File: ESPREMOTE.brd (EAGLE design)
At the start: 48 x 78 mm, 37 parts, among them IC1 ESP12SMT, IC2 LD111733, J1 DC_2_1MM, Q1 2N7002, Q2 2N7002, Q3 2N7002, Q4 2N7002

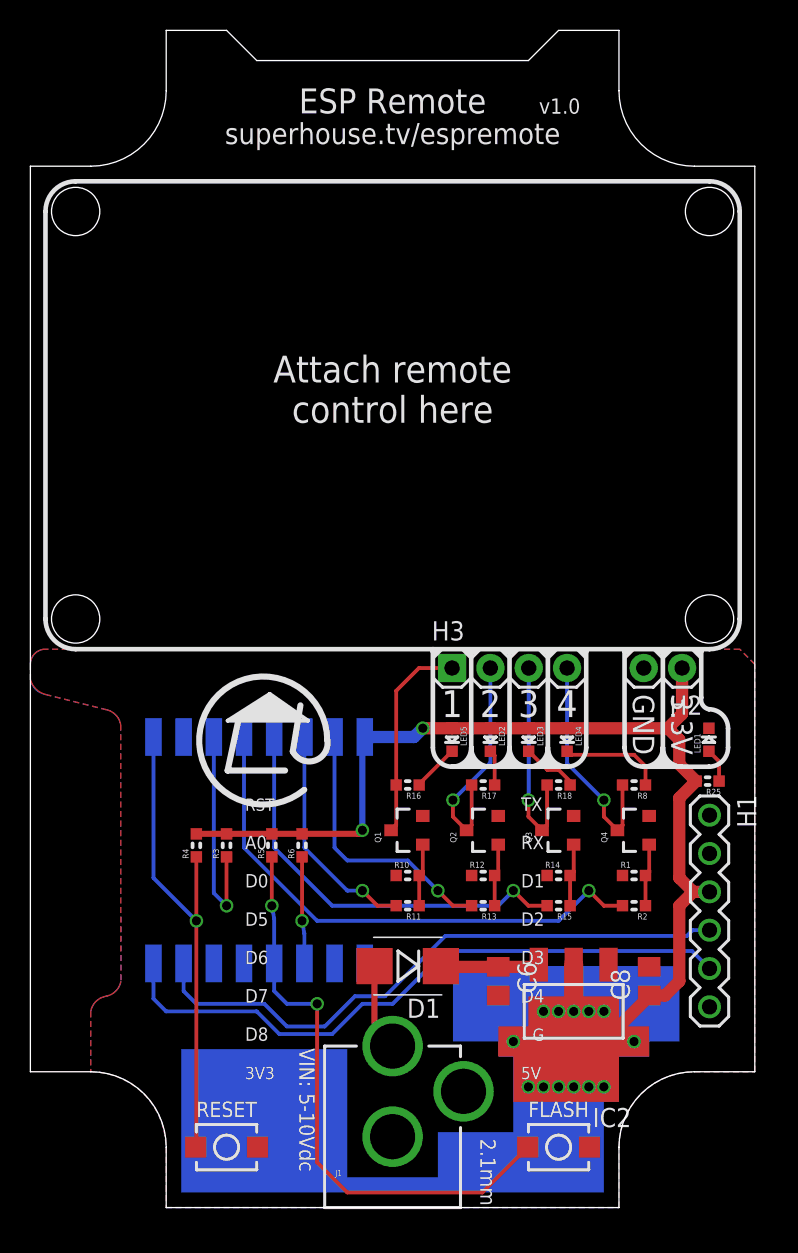
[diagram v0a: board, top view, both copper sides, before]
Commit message: Finished schematic and routing for v1.0 release
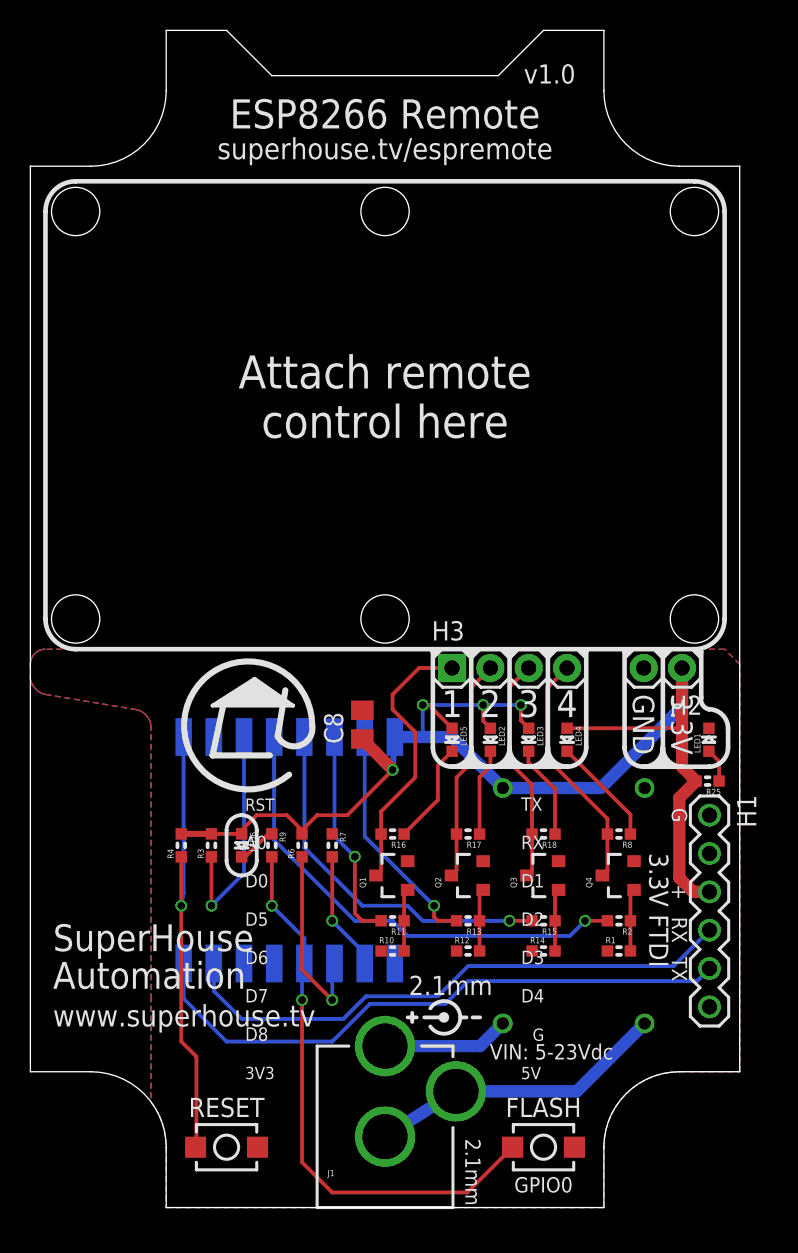
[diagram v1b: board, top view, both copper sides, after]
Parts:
- removed C6: 10uF 10V 0805, freetronics-jon:C0805
- removed D1: 1N4004 SMB, freetronics:SMB-DIODE
- removed R5: 10k, freetronics-jon:0603
- added LED6: CH1/RED, freetronics-master-v1:LED-0603
- added R7: 10k, freetronics-jon:0603
- added R9: 1K, freetronics-master-v1:0603
- IC2: value LD111733 -> REGMODULE4PIN; device freetronics-luke:SOT-223 -> freetronics-jon:REGMODULE4PIN
- moved C8 25.5 mm to (22.0, 32.0)
- moved IC2 7.00 mm to (36.0, 20.0), flipped to the bottom, turned to 90 degrees
- moved R1 5.10 mm to (39.0, 17.0)
- moved R10 5.10 mm to (24.0, 17.0)
- moved R12 5.10 mm to (29.0, 17.0)
- moved R14 5.10 mm to (34.0, 17.0)
- moved R16 3.40 mm to (24.0, 24.8)
- moved R17 3.40 mm to (29.0, 24.8)
- moved R18 3.40 mm to (34.0, 24.8)
- moved R8 3.40 mm to (39.0, 24.8)
- moved Q1 3.16 mm to (24.0, 22.0)
- moved Q2 3.16 mm to (29.0, 22.0)
- moved Q3 3.16 mm to (34.0, 22.0)
- moved Q4 3.16 mm to (39.0, 22.0)
- moved IC1 2.00 mm to (14.2, 23.7)
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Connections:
- removed net VIN: C6.1, D1.C, IC2.3
- new net N$27: LED6.C, R9.1
- new net N$28: IC2.1, J1.GND, J1.GNDBREAK
- net 3.3V: now also IC2.3, LED6.A; no longer IC2.2, IC2.4, R5.2
- net GND: now also IC2.4, R7.1; no longer C6.2, IC2.1, J1.GND, J1.GNDBREAK
- net GPIO0: now also R9.2; no longer R5.1
- net GPIO15: now also R7.2
- net N$8: now also IC2.2; no longer D1.A
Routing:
- net N$28: track 0.00 -> 19.9 mm
- net 3.3V: track 77.4 -> 87.0 mm, vias 3 -> 4
- net GPIO15: track 0.00 -> 7.95 mm, vias 0 -> 1
- net VIN: track 6.57 -> 0.00 mm
- net GPIO2: track 7.07 -> 12.8 mm
- net N$5: track 13.7 -> 18.4 mm
- net GPIO16: track 35.7 -> 32.0 mm
- net N$24: track 3.14 -> 6.80 mm
- net N$21: track 2.35 -> 5.79 mm
- net GPIO14: track 27.8 -> 24.4 mm
- net N$27: track 0.00 -> 2.63 mm
- net N$8: track 5.80 -> 8.42 mm
- net GPIO13: track 18.0 -> 15.4 mm
- net TX: track 42.9 -> 40.4 mm
- net N$4: track 3.81 -> 6.23 mm
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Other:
- board size 48 x 78 mm -> 47 x 78 mm
- board text added: "+"
- board text added: "3.3V FTDI"
- board text added: "ESP8266 Remote"
- board text added: "GPIO0"
- board text added: "Licensed under the terms of the TAPR Open Hardware Licence: tapr.org/ohl"
- board text added: "SuperHouse Automation"
- board text added: "VIN: 5-23Vdc"
- board text added: "www.superhouse.tv"
- board text removed: "ESP Remote"
- board text removed: "VIN: 5-10Vdc"

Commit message: Final silkscreen and label improvements for v1.0 release
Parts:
- LED6: value CH1/RED -> GREEN

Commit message: Added output info to silkscreen
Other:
- board text added: "Arduino board profile: "Generic ESP8266 Module""
- board text added: "Licensed under the TAPR Open Hardware Licence: tapr.org/ohl"
- board text added: "Output 1: GPIO12 Output 2: GPIO13 Output 3: GPIO14 Output 4: GPIO16"
- board text removed: "Arduino board profile: Generic ESP8266"
- board text removed: "Licensed under the terms of the TAPR Open Hardware Licence: tapr.org/ohl"
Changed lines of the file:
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@@
 <layer number="14" name="Route14" color="1" fill="6" visible="no" active="no"/>
 <layer number="15" name="Route15" color="4" fill="6" visible="no" active="no"/>
-<layer number="16" name="Bottom" color="1" fill="1" visible="no" active="yes"/>
+<layer number="16" name="Bottom" color="1" fill="1" visible="yes" active="yes"/>
 <layer number="17" name="Pads" color="2" fill="1" visible="yes" active="yes"/>
 <layer number="18" name="Vias" color="2" fill="1" visible="yes" active="yes"/>
 <layer number="19" name="Unrouted" color="12" fill="1" visible="yes" active="yes"/>
 <layer number="20" name="Dimension" color="15" fill="1" visible="yes" active="yes"/>
-<layer number="21" name="tPlace" color="15" fill="1" visible="no" active="yes"/>
-<layer number="22" name="bPlace" color="14" fill="1" visible="no" active="yes"/>
+<layer number="21" name="tPlace" color="15" fill="1" visible="yes" active="yes"/>
+<layer number="22" name="bPlace" color="14" fill="1" visible="yes" active="yes"/>
 <layer number="23" name="tOrigins" color="15" fill="1" visible="yes" active="yes"/>
 <layer number="24" name="bOrigins" color="3" fill="1" visible="yes" active="yes"/>
@@
 <text x="14.224" y="13.589" size="0.889" layer="25" font="vector" ratio="15">D7</text>
 <text x="14.224" y="21.209" size="0.889" layer="25" font="vector" ratio="15">D0</text>
-<text x="34.186" y="52.9" size="1.27" layer="22" font="vector" ratio="12" distance="36" rot="MR0">(C)2017 SuperHouse
+<text x="35.186" y="67.9" size="1.5" layer="22" font="vector" ratio="12" distance="36" rot="MR0">(C)2017 SuperHouse
 Automation Pty Ltd</text>
 <text x="23.5" y="71.5" size="1.9304" layer="21" font="vector" ratio="18" distance="40" rot="SR0" align="bottom-center">ESP8266 Remote</text>
@@
 <text x="30.438" y="9.814" size="1.016" layer="21" font="vector" ratio="13" rot="SR0">VIN: 5-23Vdc</text>
 <text x="13" y="6" size="1.27" layer="21" font="vector" ratio="18" distance="40" rot="SR0" align="bottom-center">RESET</text>
-<text x="34.186" y="61.158" size="1.27" layer="22" font="vector" ratio="15" rot="MR0">Arduino board profile:
-Generic ESP8266</text>
+<text x="40.186" y="59.158" size="1.7" layer="22" font="vector" ratio="15" rot="MR0">Arduino board profile:
+"Generic ESP8266 Module"</text>
 <wire x1="46" y1="66" x2="44" y2="68" width="0.3048" layer="21" curve="90"/>
 <wire x1="44" y1="68" x2="3" y2="68" width="0.3048" layer="21"/>
@@
 Automation</text>
 <text x="1.5" y="12" size="1.4224" layer="21" font="vector" ratio="15">www.superhouse.tv</text>
-<text x="34.186" y="44.158" size="1.27" layer="22" font="vector" ratio="15" rot="MR0">Licensed under the
-terms of the TAPR
-Open Hardware Licence:
-tapr.org/ohl</text>
+<text x="40.186" y="42.158" size="1.3" layer="22" font="vector" ratio="15" rot="MR0">Licensed under the TAPR Open
+Hardware Licence: tapr.org/ohl</text>
 <circle x="42" y="11" radius="0.5" width="0.5" layer="22"/>
 <hole x="23.5" y="66" drill="3.2"/>
@@
 <wire x1="14" y1="22" x2="15" y2="23" width="0.254" layer="21" curve="90"/>
 <wire x1="15" y1="23" x2="15" y2="25" width="0.254" layer="21"/>
+<text x="34.186" y="49.158" size="1.5" layer="22" font="vector" ratio="15" distance="40" rot="MR0">Output 1: GPIO12
+Output 2: GPIO13
+Output 3: GPIO14
+Output 4: GPIO16</text>
 </plain>
 <attributes>

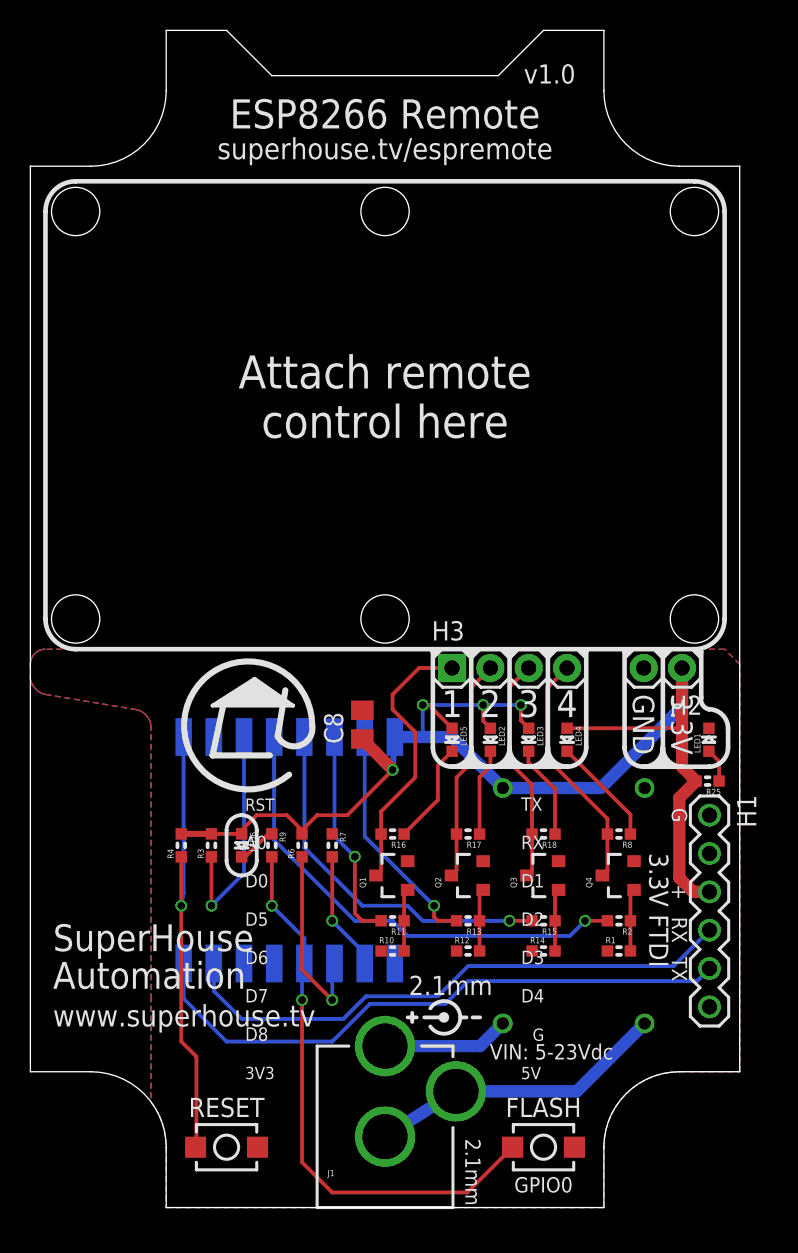
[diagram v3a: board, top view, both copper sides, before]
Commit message: Changed output 4 from GPIO16 to GPIO4
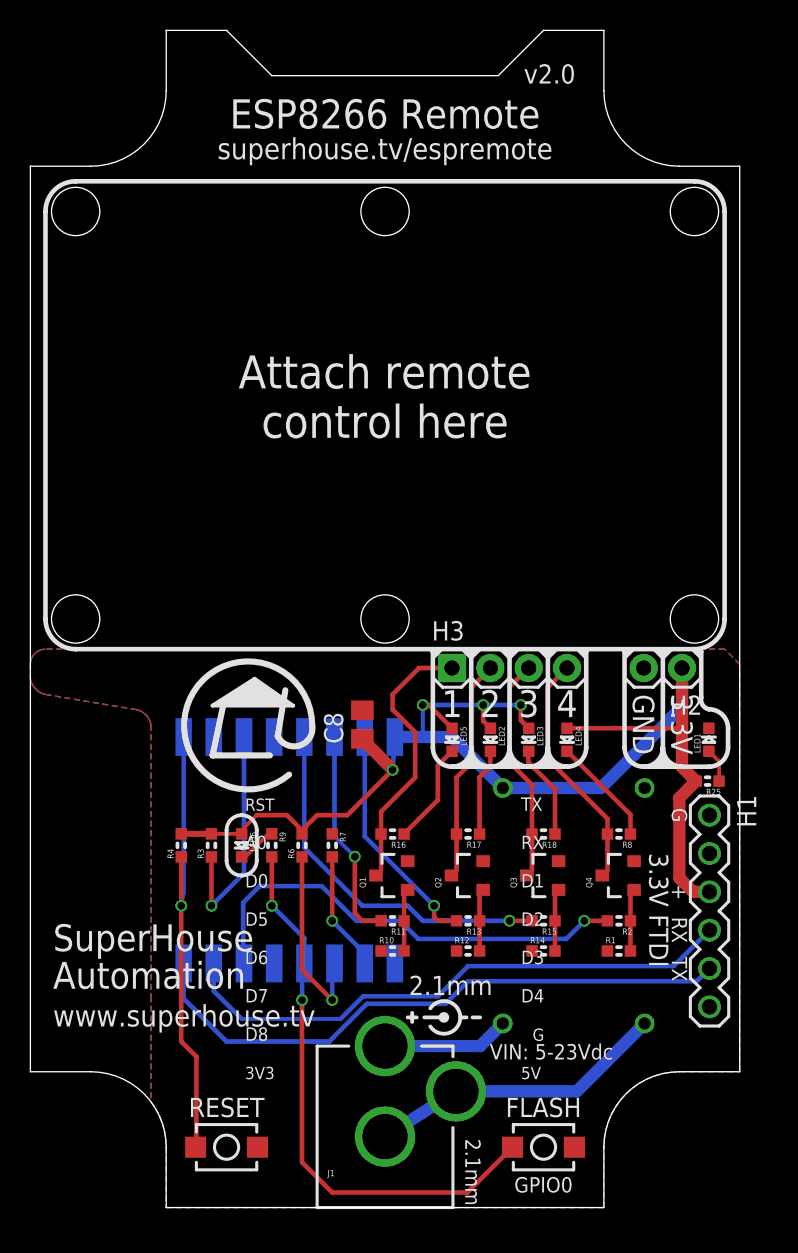
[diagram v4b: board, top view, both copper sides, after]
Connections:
- net GPIO16: no longer R2.2
- net GPIO4: now also R2.2
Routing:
- net GPIO16: track 32.0 -> 0.00 mm, vias 1 -> 0
- net GPIO4: track 0.00 -> 30.6 mm, vias 0 -> 1
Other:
- board text added: "Output 1: GPIO12 Output 2: GPIO13 Output 3: GPIO14 Output 4: GPIO4"
- board text added: "v2.0"
- board text removed: "Output 1: GPIO12 Output 2: GPIO13 Output 3: GPIO14 Output 4: GPIO16"
- board text removed: "v1.0"

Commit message: Replaced 2.1mm DC jack and switchmode reg with USB socket and linear reg
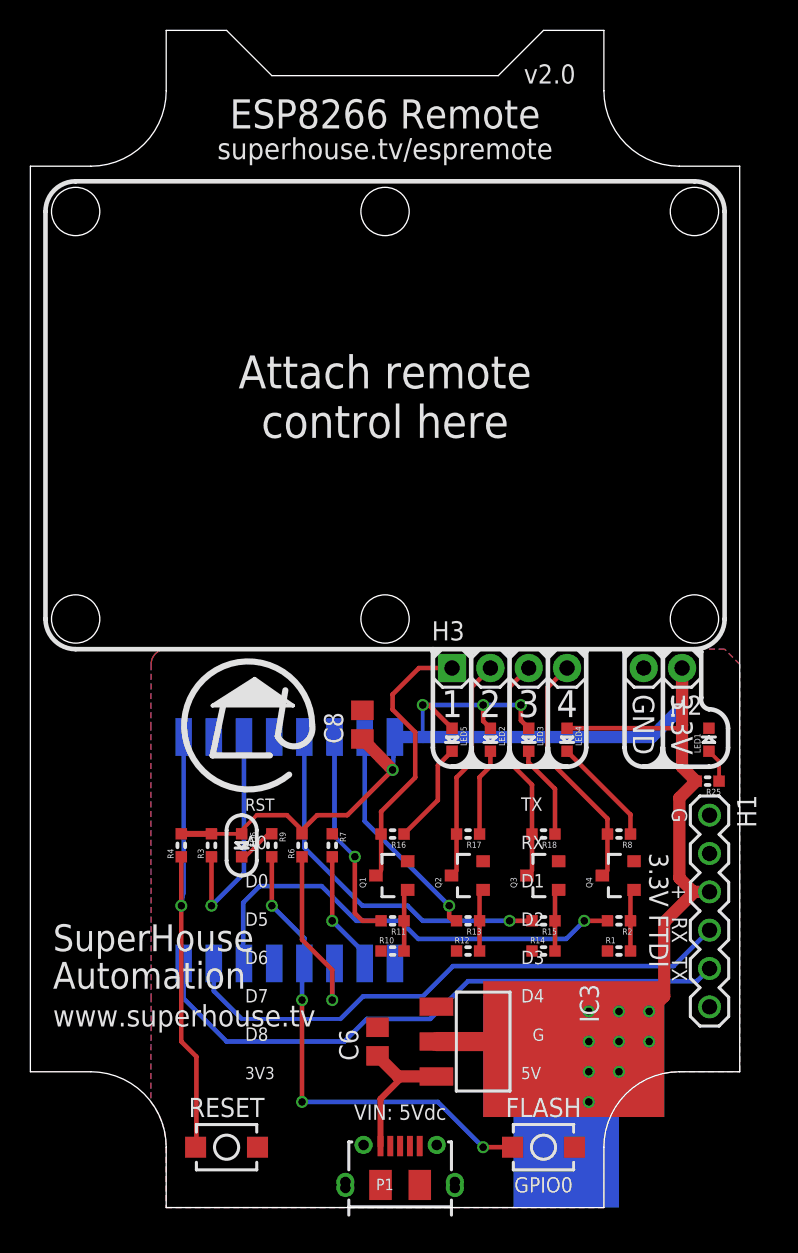
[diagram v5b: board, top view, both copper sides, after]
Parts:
- removed IC2: REGMODULE4PIN, freetronics-jon:REGMODULE4PIN
- removed J1: DC_2_1MM, freetronics:POWER_JACK_PTH
- added C6: 10uF 10V 0805, freetronics-jon:C0805
- added IC3: LD111733, freetronics-luke:SOT-223
- added P1: USB-6PSMT, freetronics-jon:USB-MICROB-MB05PMXX
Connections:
- removed net N$28: IC2.1, J1.GND, J1.GNDBREAK
- removed net N$8: IC2.2, J1.PWR
- new net 5V: C6.1, IC3.3, P1.VBUS
- net 3.3V: now also IC3.2, IC3.4; no longer IC2.3
- net GND: now also C6.2, IC3.1, P1.FIX1, P1.FIX2, P1.GND, P1.PIN1, P1.PIN2, P1.TAB1, P1.TAB2; no longer IC2.4
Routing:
- net 3.3V: track 87.0 -> 122.3 mm, vias 4 -> 13
- net N$28: track 19.9 -> 0.00 mm
- net 5V: track 0.00 -> 9.94 mm
- net N$8: track 8.42 -> 0.00 mm
- net GPIO0: track 37.2 -> 32.4 mm, vias 2 -> 4
- net GPIO13: track 15.4 -> 14.8 mm
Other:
- board text added: "VIN: 5Vdc"
- board text removed: "2.1mm"
- board text removed: "VIN: 5-23Vdc"
